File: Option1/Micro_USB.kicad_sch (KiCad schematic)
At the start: 14 parts, among them J1401 10118194-0001LF, Q1401 BC817-40, Q1402 BC817-40, U1401 CH340X

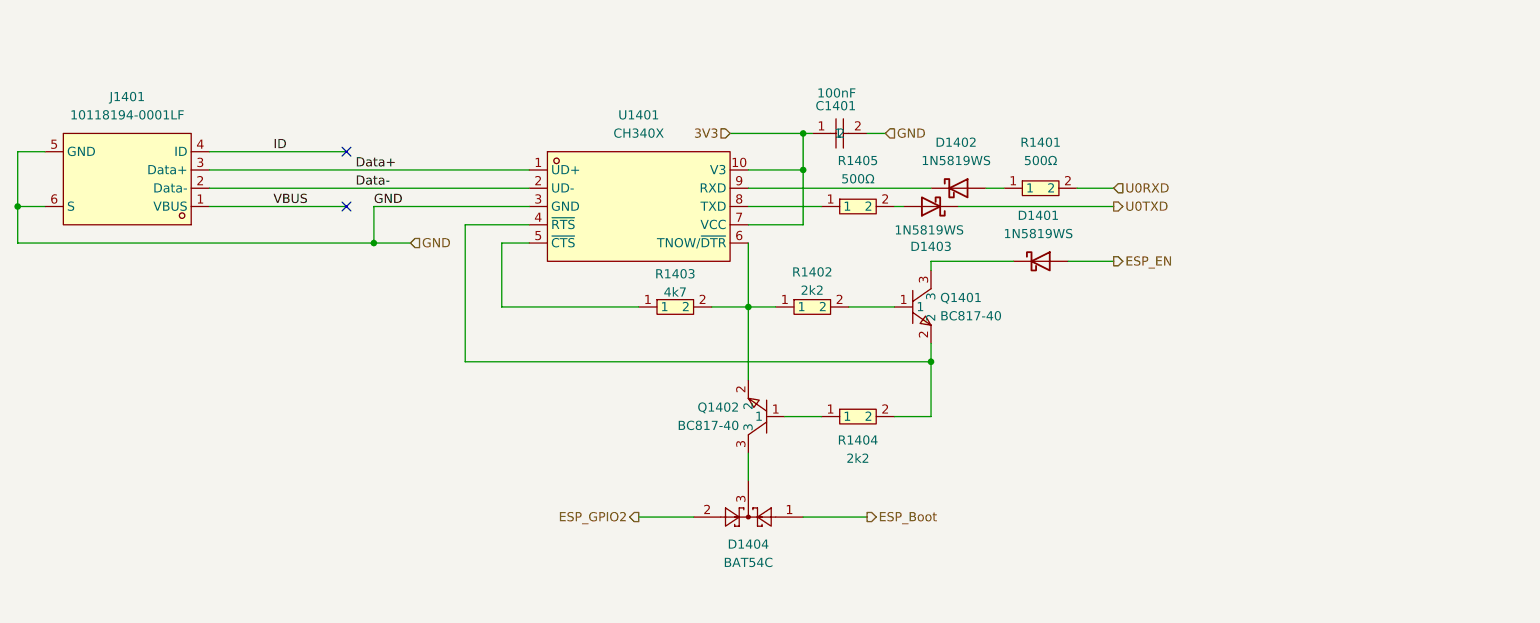
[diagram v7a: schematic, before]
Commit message: Programming Header hinzugefügt für flashen via DevKit
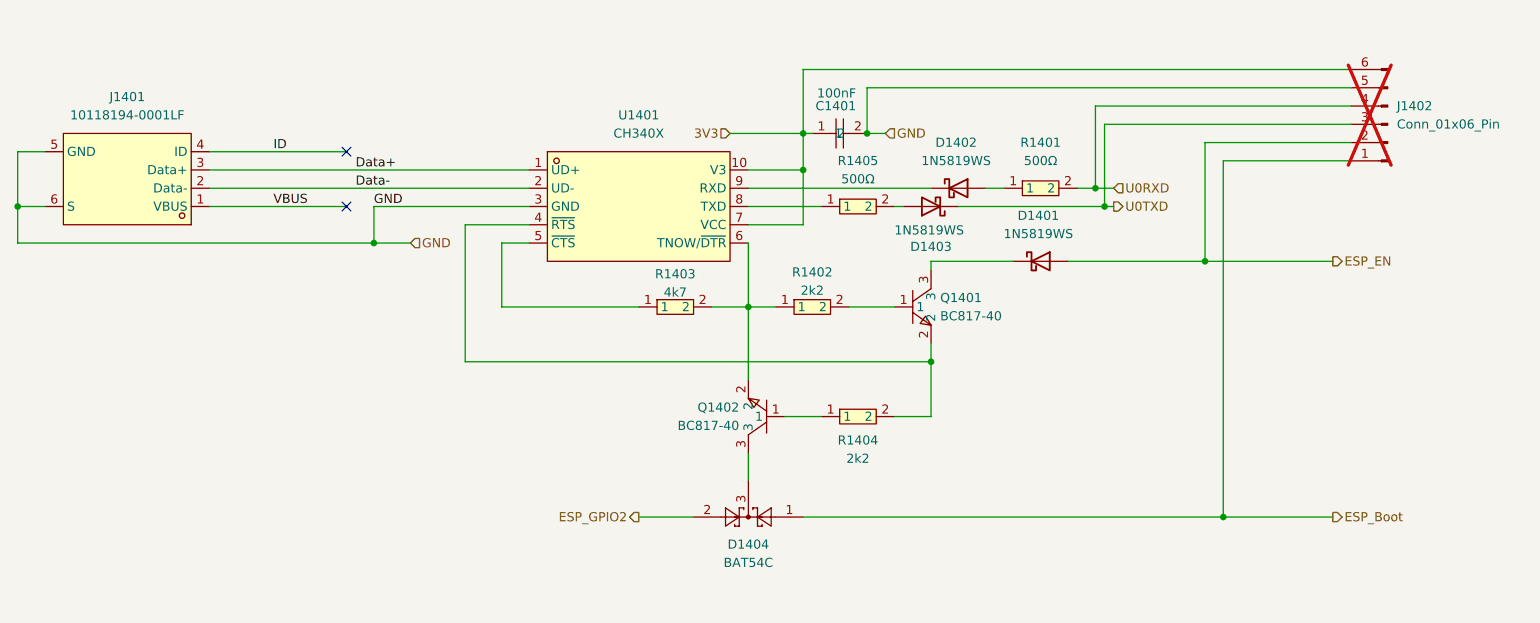
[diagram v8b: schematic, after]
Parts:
- added J1402: Conn_01x06_Pin, Connector_PinSocket_2.54mm:PinSocket_1x06_P2.54mm_Vertical, symbol Connector:Conn_01x06_Pin
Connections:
- net 3V3: now also J1402.6 (Pin_6)
- net ESP_Boot: now also J1402.1 (Pin_1)
- net ESP_EN: now also J1402.2 (Pin_2)
- net GND: now also J1402.5 (Pin_5)
- net U0RXD: now also J1402.4 (Pin_4)
- net U0TXD: now also J1402.3 (Pin_3)
